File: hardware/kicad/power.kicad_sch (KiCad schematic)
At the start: 11 parts, among them J1 1760510000, Q1 IRF4905

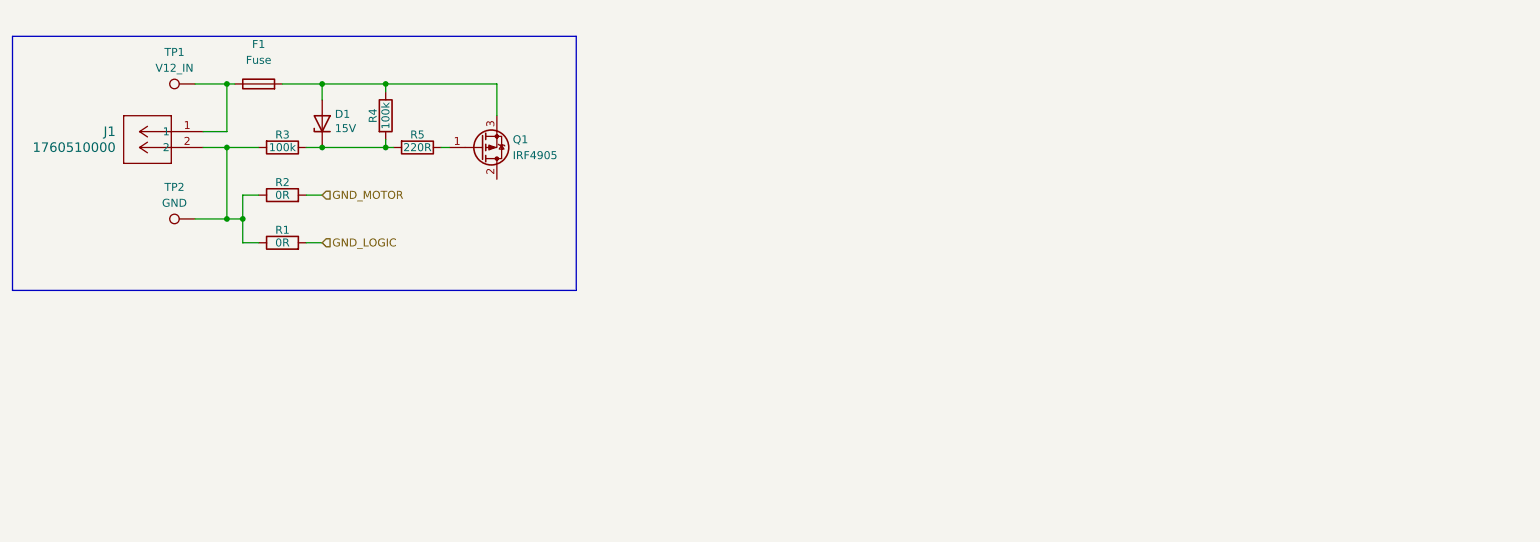
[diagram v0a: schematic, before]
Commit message: feat: added buck converter 12V to 3V3
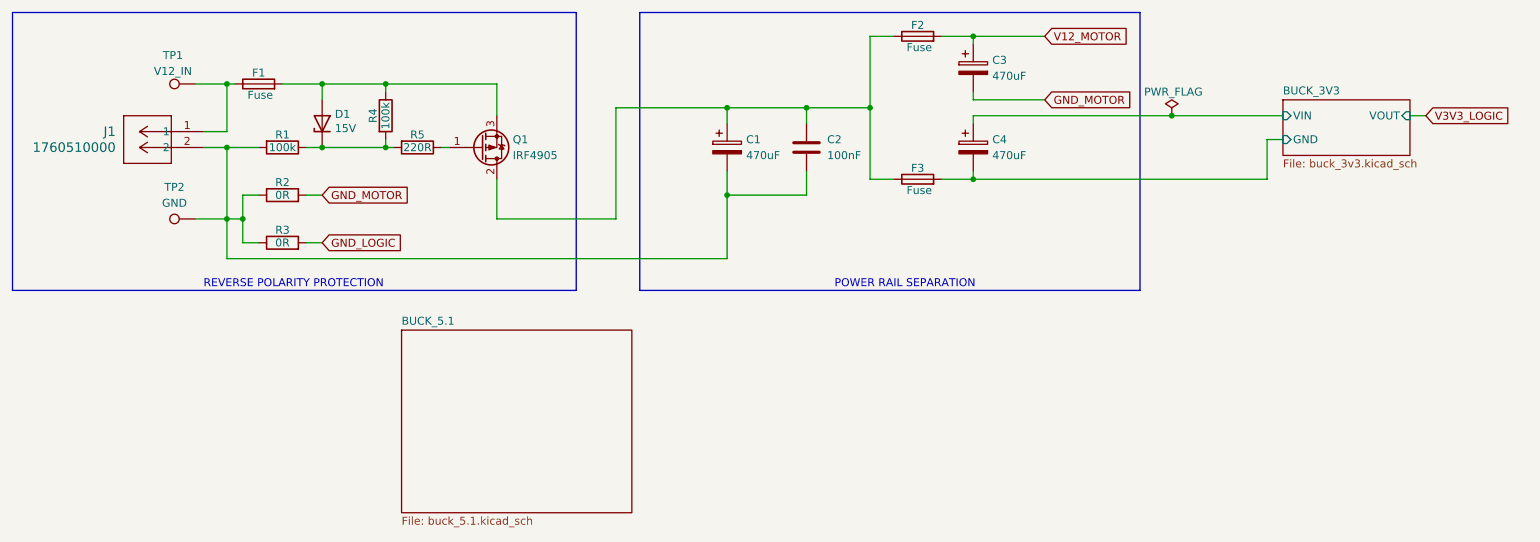
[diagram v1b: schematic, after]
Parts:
- added C1, C3, C4: 470uF, Capacitor_THT:CP_Radial_D12.5mm_P5.00mm, symbol Device:C_Polarized
- added C2: 100nF, Capacitor_THT:C_Rect_L4.0mm_W2.5mm_P2.50mm, symbol Device:C
- added F2, F3: Fuse, symbol Device:Fuse
- renumbered R3 to R1, R1 to R3
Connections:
- net GND_MOTOR: now also C3.2
- net at J1.2, R1.2, R2.1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: now also C1.2, C2.2
- net at Q1.2 (D): now also C1.1, C2.1, F2.1, F3.1
- new net BUCK_3V3/GND: C4.2, F3.2
- new net BUCK_3V3/VIN: C4.1
- new net V12_MOTOR: C3.1, F2.2
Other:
- added sheet BUCK_3V3 (buck_3v3.kicad_sch)
- added sheet BUCK_5.1 (buck_5.1.kicad_sch)
- note added: "POWER RAIL SEPARATION"
- note added: "REVERSE POLARITY PROTECTION"

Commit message: feat: added buck converter 12V to 5V
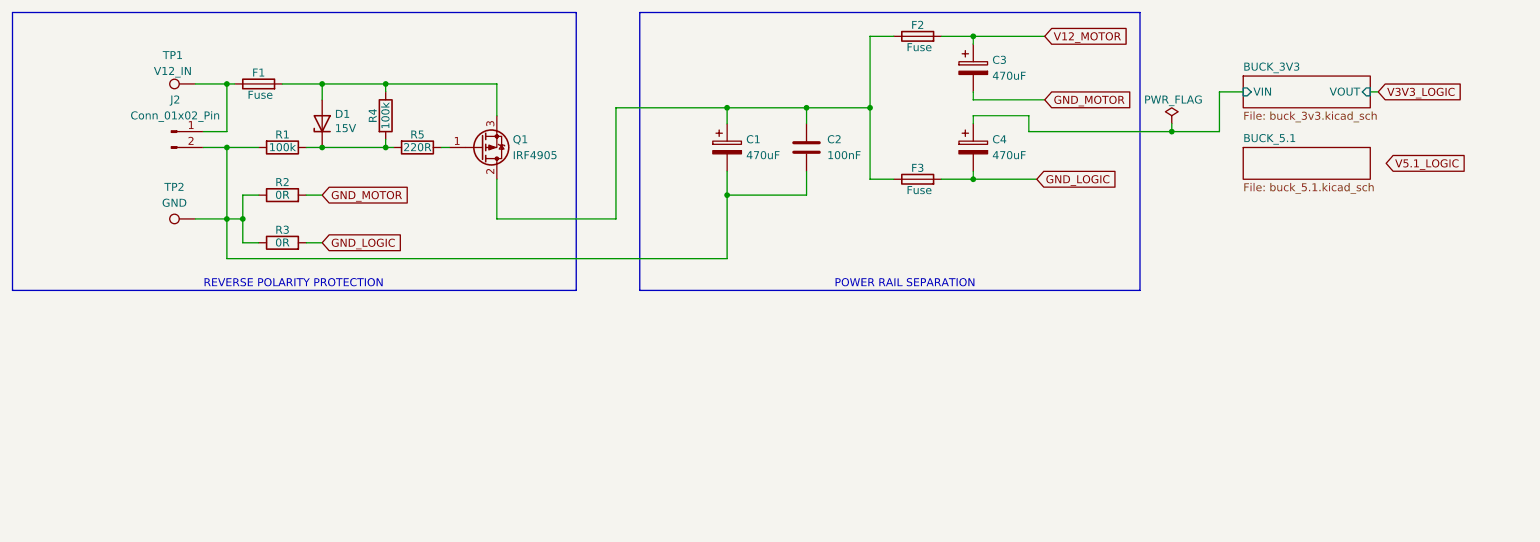
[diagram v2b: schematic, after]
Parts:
- removed J1: 1760510000, Terminal Blocks:CONN_PM 5.08&slash_02&slash_90 3.5SN BK BX_WED, symbol Terminal Blocks:1760510000
- added J2: Conn_01x02_Pin, Terminal Blocks:CONN_PM 5.08&slash_02&slash_90 3.5SN BK BX_WED, symbol Connector:Conn_01x02_Pin
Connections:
- net BUCK_3V3/GND is gone; now on net GND_LOGIC: C4.2, F3.2
- net at C1.2, C2.2, R1.2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: now also J2.2 (Pin_2)
- net at F1.1, TP1.1: now also J2.1 (Pin_1)
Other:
- sheet BUCK_3V3 ports: added none; removed GND

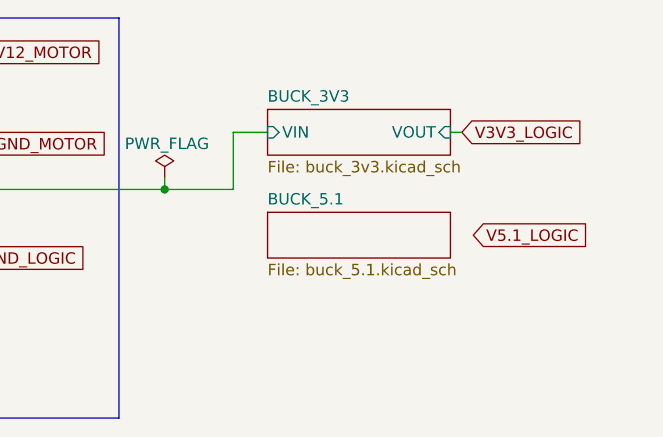
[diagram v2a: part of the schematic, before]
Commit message: fix: footprint issues and library conflicts - KiCAD
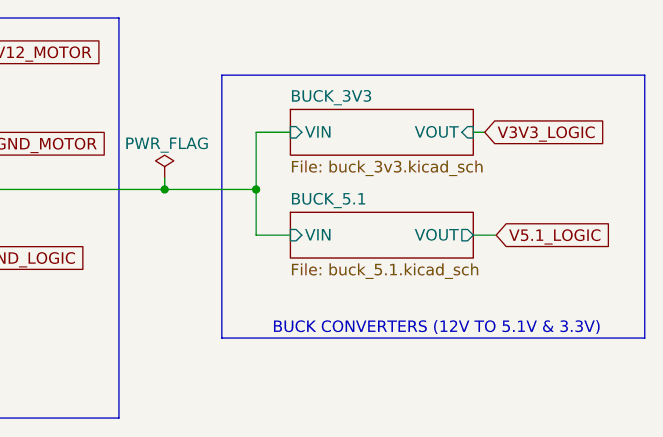
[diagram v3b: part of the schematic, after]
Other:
- sheet BUCK_5.1 ports: added VIN, VOUT; removed none
- note added: "BUCK CONVERTERS (12V TO 5.1V & 3.3V)"
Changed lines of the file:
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@@
+		)
+	)
+	(rectangle
+		(start 218.44 29.21)
+		(end 265.43 58.42)
+		(stroke
+			(width 0)
+			(type default)
+		)
+		(fill
+			(type none)
 		)
 	)
@@
 		)
 	)
+	(text "BUCK CONVERTERS (12V TO 5.1V & 3.3V)"
+		(exclude_from_sim no)
+		(at 242.316 57.404 0)
+		(effects
+			(font
+				(size 1.27 1.27)
+			)
+		)
+	)
 	(text "POWER RAIL SEPARATION"
 		(exclude_from_sim no)
@@
 	)
 	(junction
+		(at 222.25 41.91)
+		(diameter 0)
+		(color 0 0 0 0)
+	)
+	(junction
 		(at 76.2 34.29)
 		(diameter 0)
@@
 	(wire
 		(pts
-			(xy 219.71 35.56) (xy 219.71 41.91)
+			(xy 222.25 35.56) (xy 222.25 41.91)
 		)
 		(stroke
@@
 	(wire
 		(pts
-			(xy 243.84 35.56) (xy 245.11 35.56)
+			(xy 246.38 35.56) (xy 247.65 35.56)
 		)
 		(stroke
@@
 	(wire
 		(pts
-			(xy 219.71 41.91) (xy 212.09 41.91)
+			(xy 222.25 41.91) (xy 212.09 41.91)
 		)
 		(stroke
@@
 	(wire
 		(pts
+			(xy 222.25 41.91) (xy 222.25 46.99)
+		)
+		(stroke
+			(width 0)
+			(type default)
+		)
+	)
+	(wire
+		(pts
 			(xy 86.36 43.18) (xy 86.36 44.45)
 		)
@@
 	(wire
 		(pts
+			(xy 226.06 46.99) (xy 222.25 46.99)
+		)
+		(stroke
+			(width 0)
+			(type default)
+		)
+	)
+	(wire
+		(pts
 			(xy 57.15 44.45) (xy 60.96 44.45)
 		)
@@
 	(wire
 		(pts
-			(xy 219.71 35.56) (xy 223.52 35.56)
+			(xy 222.25 35.56) (xy 226.06 35.56)
 		)
 		(stroke
@@
 		(pts
 			(xy 69.85 34.29) (xy 76.2 34.29)
+		)
+		(stroke
+			(width 0)
+			(type default)
+		)
+	)
+	(wire
+		(pts
+			(xy 246.38 46.99) (xy 248.92 46.99)
 		)
 		(stroke
@@
 	(global_label "V3V3_LOGIC"
 		(shape input)
-		(at 245.11 35.56 0)
+		(at 247.65 35.56 0)
 		(fields_autoplaced yes)
 		(effects
@@
 		)
 		(property "Intersheetrefs" "${INTERSHEET_REFS}"
-			(at 259.1624 35.56 0)
+			(at 261.7024 35.56 0)
 			(effects
 				(font
@@
 	(global_label "V5.1_LOGIC"
 		(shape input)
-		(at 246.38 46.99 0)
+		(at 248.92 46.99 0)
 		(fields_autoplaced yes)
 		(effects
@@
 		)
 		(property "Intersheetrefs" "${INTERSHEET_REFS}"
-			(at 259.9486 46.99 0)
+			(at 262.4886 46.99 0)
 			(effects
 				(font
@@
 	)
 	(sheet
-		(at 223.52 44.45)
+		(at 226.06 44.45)
 		(size 20.32 5.08)
 		(exclude_from_sim no)
@@
 		)
 		(property "Sheetname" "BUCK_5.1"
-			(at 223.52 43.7384 0)
+			(at 226.06 43.7384 0)
 			(effects
 				(font
@@
 		)
 		(property "Sheetfile" "buck_5.1.kicad_sch"
-			(at 223.52 50.1146 0)
+			(at 226.06 50.1146 0)
 			(effects
 				(font
@@
 				)
 				(justify left top)
+			)
+		)
+		(pin "VIN" input
+			(at 226.06 46.99 180)
+			(effects
+				(font
+					(size 1.27 1.27)
+				)
+				(justify left)
+			)
+		)
+		(pin "VOUT" output
+			(at 246.38 46.99 0)
+			(effects
+				(font
+					(size 1.27 1.27)
+				)
+				(justify right)
 			)
 		)
@@
 	)
 	(sheet
-		(at 223.52 33.02)
+		(at 226.06 33.02)
 		(size 20.32 5.08)
 		(exclude_from_sim no)
@@
 		)
 		(property "Sheetname" "BUCK_3V3"
-			(at 223.52 32.3084 0)
+			(at 226.06 32.3084 0)
 			(effects
 				(font
@@
 		)
 		(property "Sheetfile" "buck_3v3.kicad_sch"
-			(at 223.52 38.6846 0)
+			(at 226.06 38.6846 0)
 			(effects
 				(font
@@
 		)
 		(pin "VIN" input
-			(at 223.52 35.56 180)
+			(at 226.06 35.56 180)
 			(effects
 				(font
@@
 		)
 		(pin "VOUT" input
-			(at 243.84 35.56 0)
-			(effects
-				(font
+			(at 246.38 35.56 0)
+			(effects
+				(font

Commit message: fix: protection circuit - MOSFET & enable config
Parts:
- TP1, TP2: footprint (none) -> TestPoint:TestPoint_THTPad_2.0x2.0mm_Drill1.0mm
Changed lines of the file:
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@@
 			)
 		)
-		(property "Footprint" ""
+		(property "Footprint" "TestPoint:TestPoint_THTPad_2.0x2.0mm_Drill1.0mm"
 			(at 55.88 50.8 0)
 			(effects
@@
 			)
 		)
-		(property "Footprint" ""
+		(property "Footprint" "TestPoint:TestPoint_THTPad_2.0x2.0mm_Drill1.0mm"
 			(at 55.88 29.21 0)
 			(effects
